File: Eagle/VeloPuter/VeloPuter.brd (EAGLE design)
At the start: 101.3 x 64.1 mm, 56 parts, among them IC2 B7546, IC3 B7546, Q1 4P04L04, Q10 4P04L04, Q11 BS170, Q12 4P04L04, Q13 BS170, Q14 4P04L04, Q2 BS170, Q3 BS170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

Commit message: Minor layout change
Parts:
- moved IC3 1.31 mm to (76.8, 54.9)
- moved C1 0.71 mm to (70.5, 56.2)
- moved C2 0.64 mm to (68.6, 21.0)
- moved R6 0.64 mm to (76.2, 31.1)
- moved D1 0.63 mm to (76.2, 17.8)
- moved DC1 0.32 mm to (75.6, 43.5)
- moved SP2 0.32 mm to (66.4, 6.99)
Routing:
- net V+: track 100.9 -> 103.4 mm
- net VDD: track 193.7 -> 192.3 mm
- net V-: track 15.1 -> 16.5 mm
- net N$1: track 31.3 -> 30.6 mm
- net GND: track 6.35 -> 5.71 mm
- net BRAKE_SWITCH: track 64.6 -> 63.9 mm
- net PWM_BUZZER: track 52.6 -> 52.0 mm
- added copper zone on layer 1, net GND
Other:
- board size 101.3 x 64.1 mm -> 79.7 x 62.9 mm

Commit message: Board updates
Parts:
- R6: value 1 ohm -> 1 Ω
- renumbered JP6 to JP
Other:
- board text added: "+"
- board text added: "-"
- board text added: "Aux"
- board text added: "Brake"
- board text added: "Head"
- board text added: "In Batt 9-24V"
- board text added: "Left"
- board text added: "Out 5V"
- board text added: "Rear"
- board text added: "Right"
- board text added: "VeloPuter LED driver. rev. 1.3 Dec 2019 Docs: https://veloputer.wordpress.com/ Code: https://github.com/RodePioneer/VeloPuter/"
- board text removed: "V+"
- board text removed: "V-"
- board text removed: "VeloPuter LED driver. rev. 1.2 May 2016"
- board text removed: "https://github.com/RodePioneer/VeloPuter/"

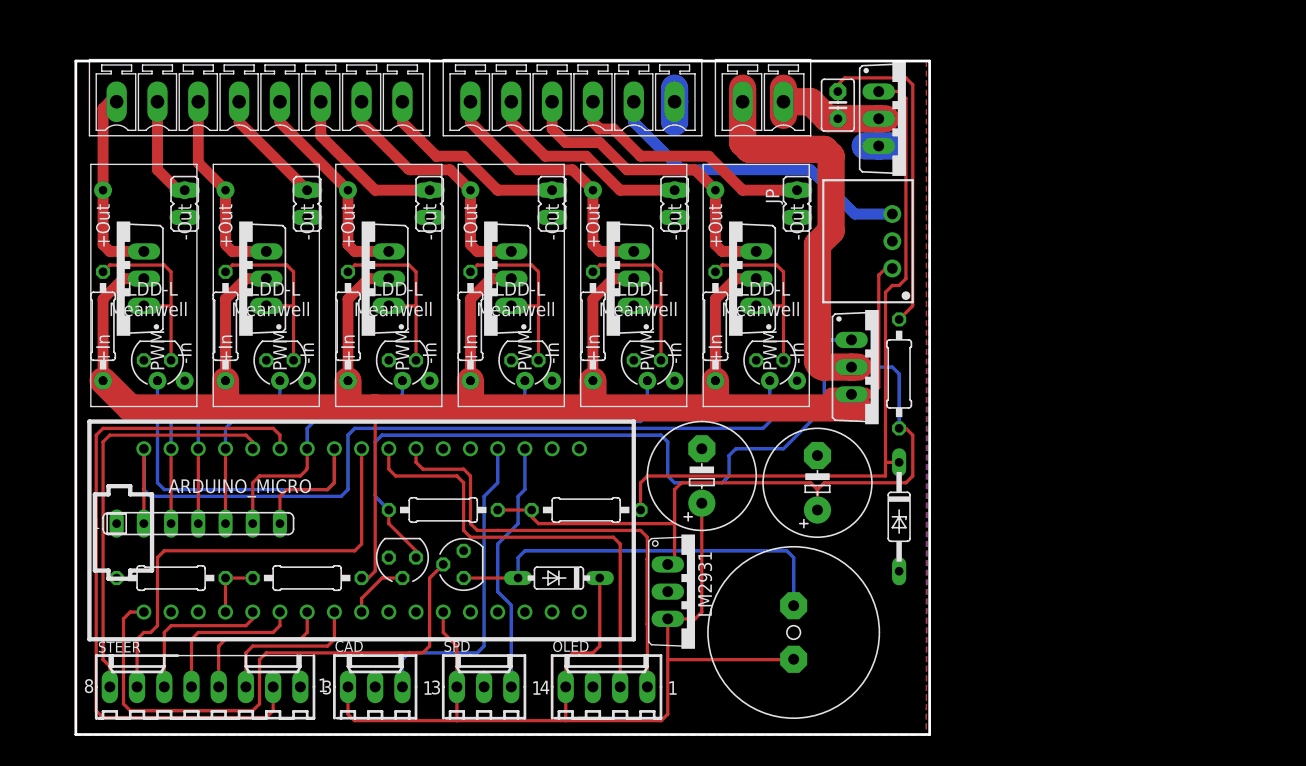
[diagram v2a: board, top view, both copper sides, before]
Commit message: Board version 1.4 Suitable for the QV with new headlights
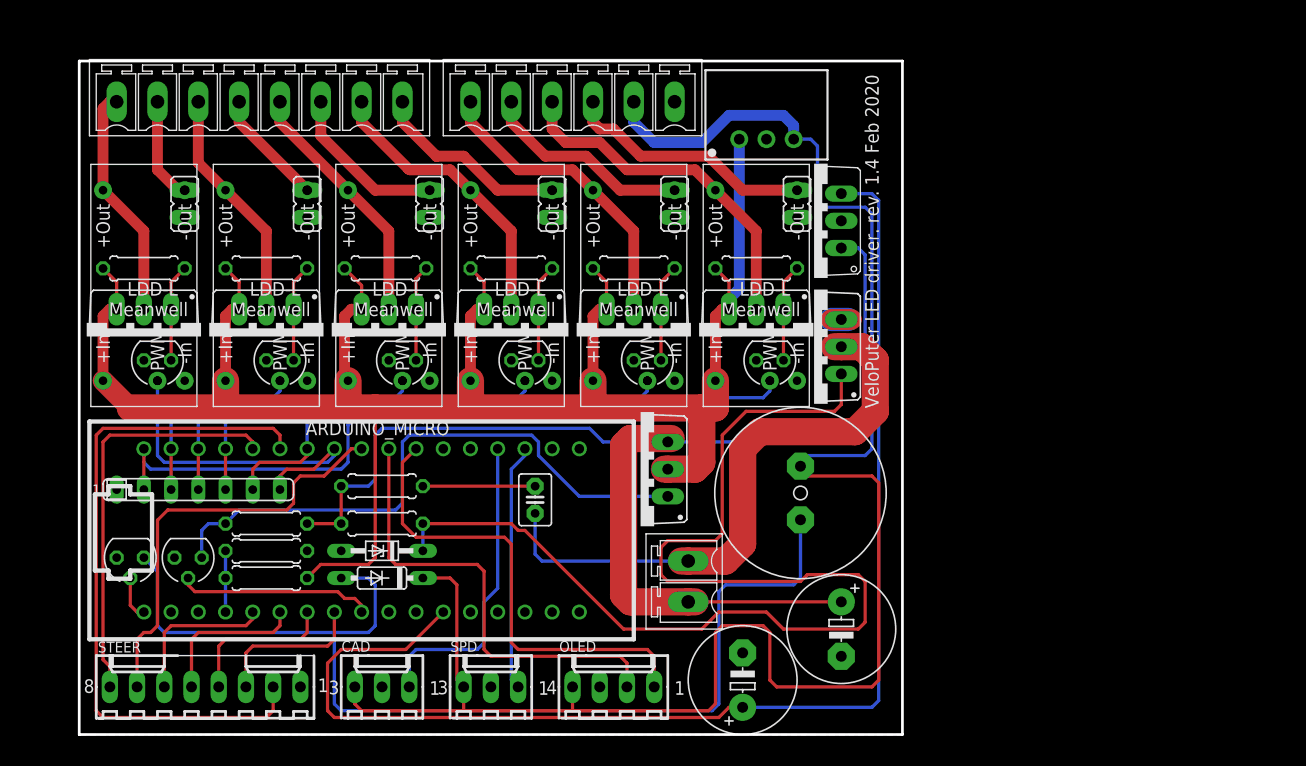
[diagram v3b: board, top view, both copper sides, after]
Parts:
- removed D1: ZPD, diode:DO35Z10
- added ZENER: Z12V, diode:DO34Z7
- IC2: value B7546 -> BS170
- LM2931: value 7805TV -> LM2931
- Q1: value 4P04L04 -> SQP50P03
- R1, R10, R11, R2, R3, R4, R5, R6, R7, R8, R9: device resistor:0207/10 -> resistor:0207/7
- VBATT: value (none) -> VBatt
- moved R6 49.4 mm to (27.9, 20.6), turned to 180 degrees
- moved C1 46.4 mm to (42.2, 19.4)
- moved VBATT 45.3 mm to (56.5, 11.7), turned to 90 degrees
- moved LM2931 36.3 mm to (68.3, 45.4), turned to 90 degrees
- moved IC2 31.1 mm to (4.45, 14.0), turned to 180 degrees
- moved Q1 24.2 mm to (52.1, 22.2), turned to 90 degrees
- moved IC3 22.9 mm to (68.3, 33.7), turned to 90 degrees
- moved Q2 20.0 mm to (9.84, 14.0)
- moved C3 19.4 mm to (61.6, 2.54)
- moved R5 19.1 mm to (27.9, 17.1)
- moved R11 16.6 mm to (17.1, 17.1)
- moved D2 16.5 mm to (27.9, 12.1)
- moved DC1 15.1 mm to (63.8, 53.0), turned to 0 degrees
- moved C2 13.8 mm to (70.8, 7.30), turned to 270 degrees
- moved SP2 13.0 mm to (67.0, 20.0), turned to 270 degrees
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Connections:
- removed net V_USB: AUX_OUT.5, DC1.3
- new net 5V_USB: AUX_OUT.5, CAD.3, D2.C, DC1.3, OLED.4, SP2.1, SPD.3
- net 5V: no longer CAD.3, D2.C, OLED.4, SP2.1, SPD.3
- net AUX1+: now also Q12.D; no longer Q12.S
- net AUX2+: now also Q14.D; no longer Q14.S
- net FRONT+: now also Q4.D; no longer Q4.S
- net GND: now also ZENER.A; no longer D1.A
- net LEFT+: now also Q8.D; no longer Q8.S
- net N$4: now also ZENER.C; no longer D1.C
- net REAR+: now also Q6.D; no longer Q6.S
- net RIGHT+: now also Q10.D; no longer Q10.S
- net V+: now also Q1.S; no longer Q1.D
- net VDD: now also Q1.D, Q10.S, Q12.S, Q14.S, Q4.S, Q6.S, Q8.S; no longer Q1.S, Q10.D, Q12.D, Q14.D, Q4.D, Q6.D, Q8.D
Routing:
- net 5V_USB: track 0.00 -> 171.0 mm
- net N$14: track 37.7 -> 102.4 mm
- net PWM_BUZZER: track 52.0 -> 4.07 mm
- net N$4: track 66.1 -> 106.3 mm
- net V-: track 16.5 -> 56.6 mm
- net V_USB: track 29.6 -> 0.00 mm
- net 5V: track 93.5 -> 120.0 mm
- net N$1: track 30.6 -> 10.5 mm
- net V+: track 103.4 -> 119.6 mm
- net N$15: track 70.8 -> 56.2 mm
- net POWER_ONOFF: track 5.87 -> 18.3 mm
- net ONOFF_AUX2: track 79.2 -> 69.8 mm
- net PWM_FRONT: track 41.1 -> 32.1 mm
- net N$23: track 17.7 -> 8.97 mm
- net N$33: track 17.7 -> 9.10 mm
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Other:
- board size 79.7 x 62.9 mm -> 76.8 x 62.9 mm
- board text added: "Docs: https://veloputer.wordpress.com/ Code: https://github.com/RodePioneer/VeloPuter/"
- board text added: "VeloPuter LED driver. rev. 1.4 Feb 2020"
- board text removed: "In Batt 9-24V"
- board text removed: "VeloPuter LED driver. rev. 1.3 Dec 2019 Docs: https://veloputer.wordpress.com/ Code: https://github.com/RodePioneer/VeloPuter/"
